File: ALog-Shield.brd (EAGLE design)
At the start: 53.3 x 78.5 mm, 25 parts, among them U1 DS3231MZ/V+T

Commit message: ALog and Made in MN back silk
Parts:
- removed U$1: ALOG_LOGO_V1_5.5MM, awickert:ALOG_LOGO_V1_SMALL
- removed U$4: NWLOGO, awickert:NWLOGO
- added LOGO1: OSHW-LOGOL, SparkFun-Aesthetics:OSHW-LOGO-L
- added U$2: MADE_IN_MN_220_SHIELD, awickert:MADE_IN_MN_SHIELD_220
- added U$3: ALOG_LOG, awickert:ALOG_LOG
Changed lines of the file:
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@@
 <text x="5.715" y="7.874" size="1.27" layer="21" rot="R90">A0</text>
 <text x="21.601" y="32.1275" size="0.6096" layer="21">TM</text>
-<text x="49.3915" y="32.146" size="0.6096" layer="21" rot="R180">TM</text>
 <text x="12.715" y="7.874" size="1.27" layer="21" rot="R90">A1</text>
 <text x="9.215" y="7.874" size="1.27" layer="21" rot="R90">3V3</text>
@@
 <element name="LED1" library="SparkFun-LED" package="LED-1206" value="" x="46.609" y="56.007"/>
 <element name="R_LED1" library="resistor" package="R0603" value="220" x="42.037" y="56.007"/>
-<element name="U$1" library="awickert" package="ALOG_LOGO_V1_SMALL" value="ALOG_LOGO_V1_5.5MM" x="20.574" y="30.48"/>
 <element name="A1" library="resistor" package="0207/10" value="" x="10.414" y="31.496"/>
-<element name="U$4" library="awickert" package="NWLOGO" value="NWLOGO" x="41.275" y="30.607"/>
 <element name="LOGO2" library="SparkFun-Aesthetics" package="OSHW-LOGO-M" value="OSHW-LOGOM" x="17.272" y="39.751"/>
 <element name="RESET" library="SparkFun-Electromechanical" package="TACTILE-PTH" value="Reset" x="49.784" y="7.62" smashed="yes" rot="R90">
@@
 <element name="C15" library="rc-master-smd" package="CECJ-CTS-031817" value="10nF" x="10.414" y="30.226" rot="R90"/>
 <element name="CLOCK_BATT" library="awickert" package="LINX_BAT-HLD-012-SMT" value="Linx BAT-HLD-012-SMT" x="6.096" y="45.72" rot="R90"/>
+<element name="U$2" library="awickert" package="MADE_IN_MN_SHIELD_220" value="MADE_IN_MN_220_SHIELD" x="42.926" y="30.226" rot="R90"/>
+<element name="U$3" library="awickert" package="ALOG_LOG" value="ALOG_LOG" x="25.146" y="35.052" rot="R90"/>
+<element name="LOGO1" library="SparkFun-Aesthetics" package="OSHW-LOGO-L" value="OSHW-LOGOL" x="-4.064" y="-45.212"/>
 </elements>
 <signals>

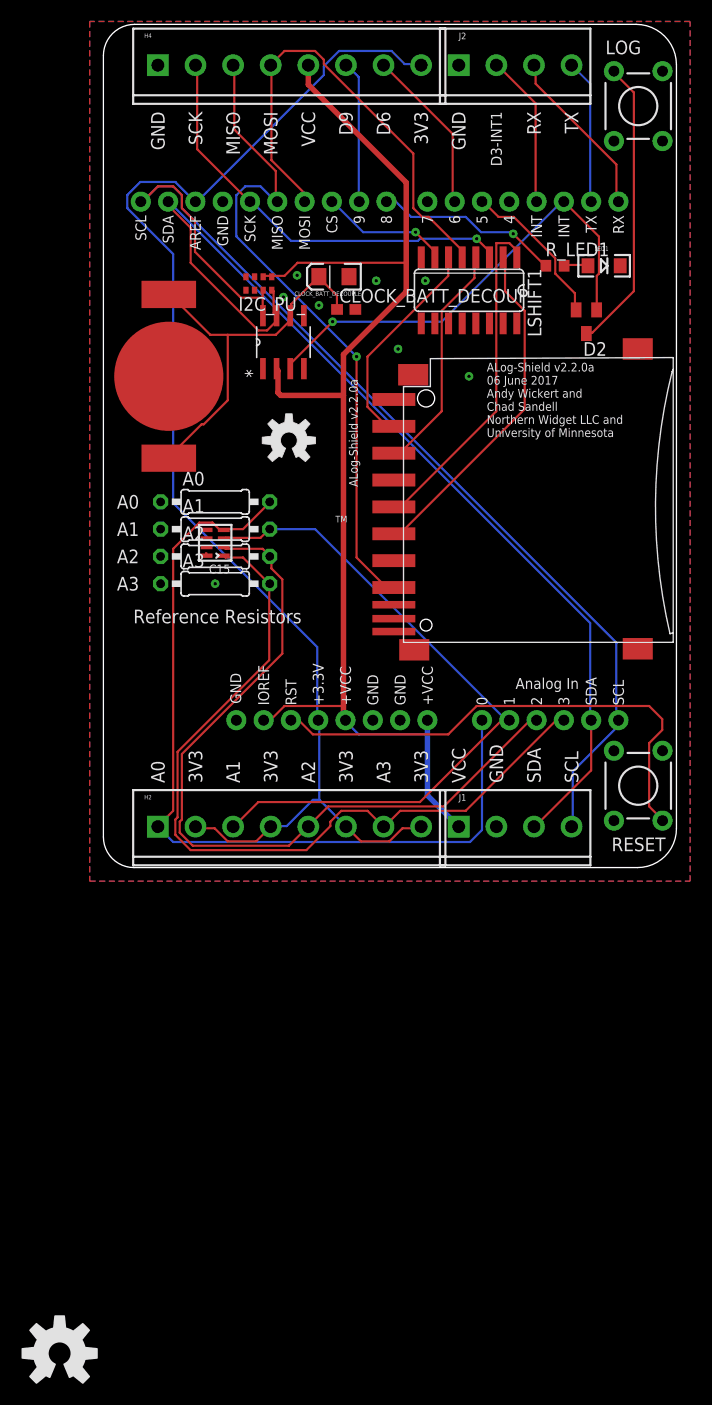
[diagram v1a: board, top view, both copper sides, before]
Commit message: Update silk and OSE logo
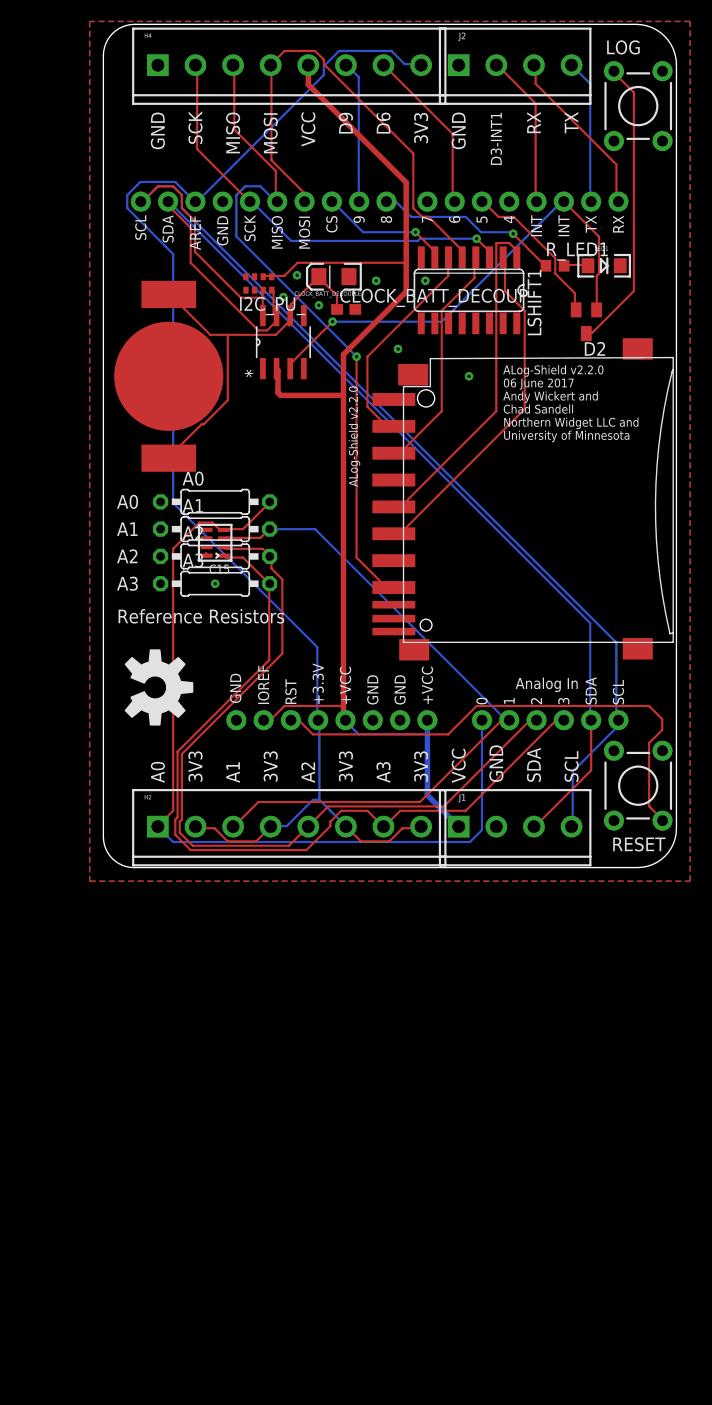
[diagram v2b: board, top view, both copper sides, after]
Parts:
- removed LOGO2: OSHW-LOGOM, SparkFun-Aesthetics:OSHW-LOGO-M
- moved LOGO1 62.6 mm to (4.83, 16.8), turned to 270 degrees
- moved U$3 5.59 mm to (19.6, 35.1)
- moved U$2 0.25 mm to (42.9, 30.5)
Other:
- board text added: "ALog-Shield v2.2.0"
- board text added: "ALog-Shield v2.2.0 06 June 2017 Andy Wickert and Chad Sandell Northern Widget LLC and University of Minnesota"
- board text removed: "ALog-Shield v2.2.0a"
- board text removed: "ALog-Shield v2.2.0a 06 June 2017 Andy Wickert and Chad Sandell Northern Widget LLC and University of Minnesota"
- board text removed: "TM"
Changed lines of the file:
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@@
 <wire x1="53.34" y1="3.62" x2="53.34" y2="74.7166" width="0" layer="20"/>
 <text x="4.445" y="70.358" size="1.27" layer="21" rot="R270">GND</text>
-<text x="35.687" y="40.0685" size="0.8128" layer="21">ALog-Shield v2.2.0a
+<text x="18.923" y="5.2705" size="0.8128" layer="22" rot="MR0">ALog-Shield v2.2.0
 06 June 2017
 Andy Wickert and
@@
 University of Minnesota</text>
 <text x="5.715" y="7.874" size="1.27" layer="21" rot="R90">A0</text>
-<text x="21.601" y="32.1275" size="0.6096" layer="21">TM</text>
 <text x="12.715" y="7.874" size="1.27" layer="21" rot="R90">A1</text>
 <text x="9.215" y="7.874" size="1.27" layer="21" rot="R90">3V3</text>
@@
 <text x="1.27" y="25.781" size="1.27" layer="21">A3</text>
 <text x="12.831" y="15.24" size="1.016" layer="21" rot="R90">GND</text>
-<text x="23.6855" y="35.433" size="0.8128" layer="21" rot="R90">ALog-Shield v2.2.0a</text>
-<text x="2.794" y="22.733" size="1.27" layer="21">Reference Resistors</text>
+<text x="23.6855" y="35.433" size="0.8128" layer="21" rot="R90">ALog-Shield v2.2.0</text>
+<text x="1.27" y="22.733" size="1.27" layer="21">Reference Resistors</text>
+<text x="37.211" y="39.8145" size="0.8128" layer="21">ALog-Shield v2.2.0
+06 June 2017
+Andy Wickert and
+Chad Sandell
+Northern Widget LLC and
+University of Minnesota</text>
 </plain>
 <attributes>
@@
 <element name="R_LED1" library="resistor" package="R0603" value="220" x="42.037" y="56.007"/>
 <element name="A1" library="resistor" package="0207/10" value="" x="10.414" y="31.496"/>
-<element name="LOGO2" library="SparkFun-Aesthetics" package="OSHW-LOGO-M" value="OSHW-LOGOM" x="17.272" y="39.751"/>
 <element name="RESET" library="SparkFun-Electromechanical" package="TACTILE-PTH" value="Reset" x="49.784" y="7.62" smashed="yes" rot="R90">
 <attribute name="PROD_ID" value=" SWCH-08441" x="218.694" y="-81.28" size="1.778" layer="27" rot="R90" display="off"/>
@@
 <element name="C15" library="rc-master-smd" package="CECJ-CTS-031817" value="10nF" x="10.414" y="30.226" rot="R90"/>
 <element name="CLOCK_BATT" library="awickert" package="LINX_BAT-HLD-012-SMT" value="Linx BAT-HLD-012-SMT" x="6.096" y="45.72" rot="R90"/>
-<element name="U$2" library="awickert" package="MADE_IN_MN_SHIELD_220" value="MADE_IN_MN_220_SHIELD" x="42.926" y="30.226" rot="R90"/>
-<element name="U$3" library="awickert" package="ALOG_LOG" value="ALOG_LOG" x="25.146" y="35.052" rot="R90"/>
-<element name="LOGO1" library="SparkFun-Aesthetics" package="OSHW-LOGO-L" value="OSHW-LOGOL" x="-4.064" y="-45.212"/>
+<element name="U$2" library="awickert" package="MADE_IN_MN_SHIELD_220" value="MADE_IN_MN_220_SHIELD" x="42.926" y="30.48" rot="R90"/>
+<element name="U$3" library="awickert" package="ALOG_LOG" value="ALOG_LOG" x="19.558" y="35.052" rot="R90"/>
+<element name="LOGO1" library="SparkFun-Aesthetics" package="OSHW-LOGO-L" value="OSHW-LOGOL" x="4.826" y="16.764" rot="R270"/>
 </elements>
 <signals>

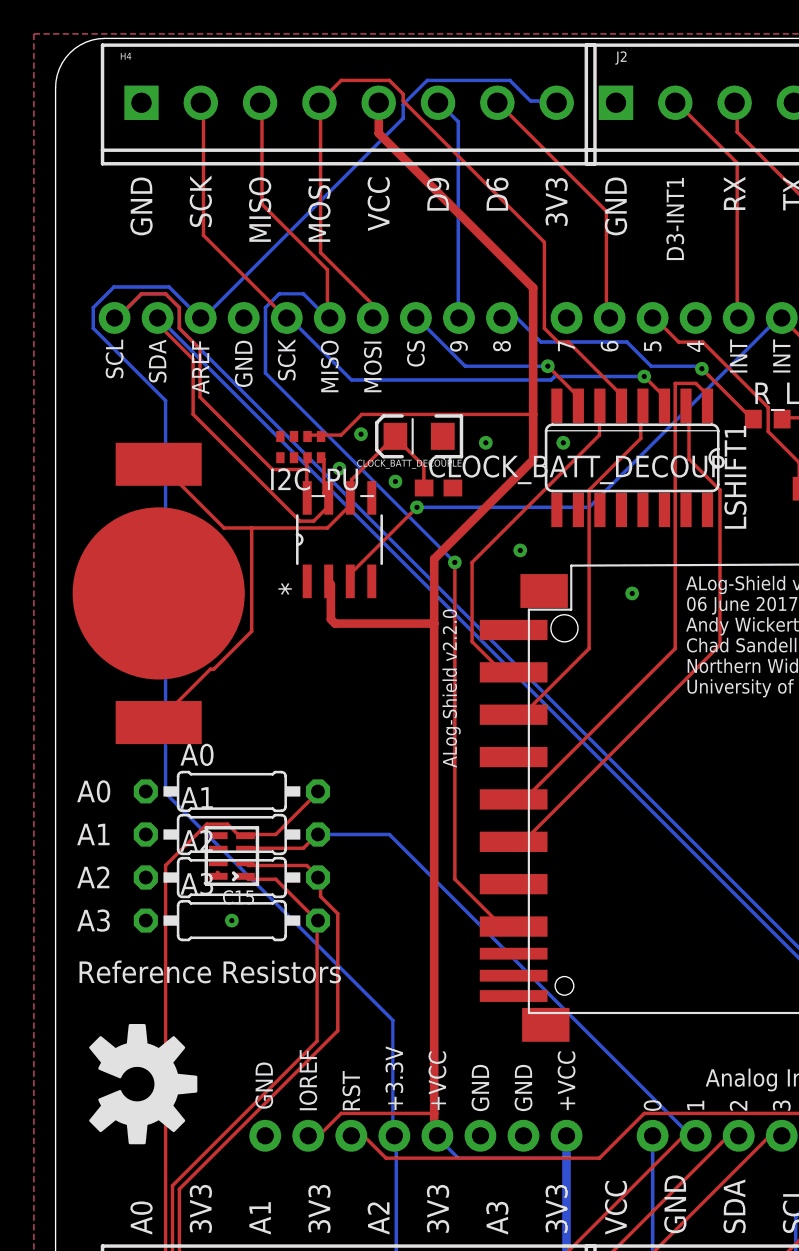
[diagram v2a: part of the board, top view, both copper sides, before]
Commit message: Added D4 and D7 out put points, will not populate with screw terminals
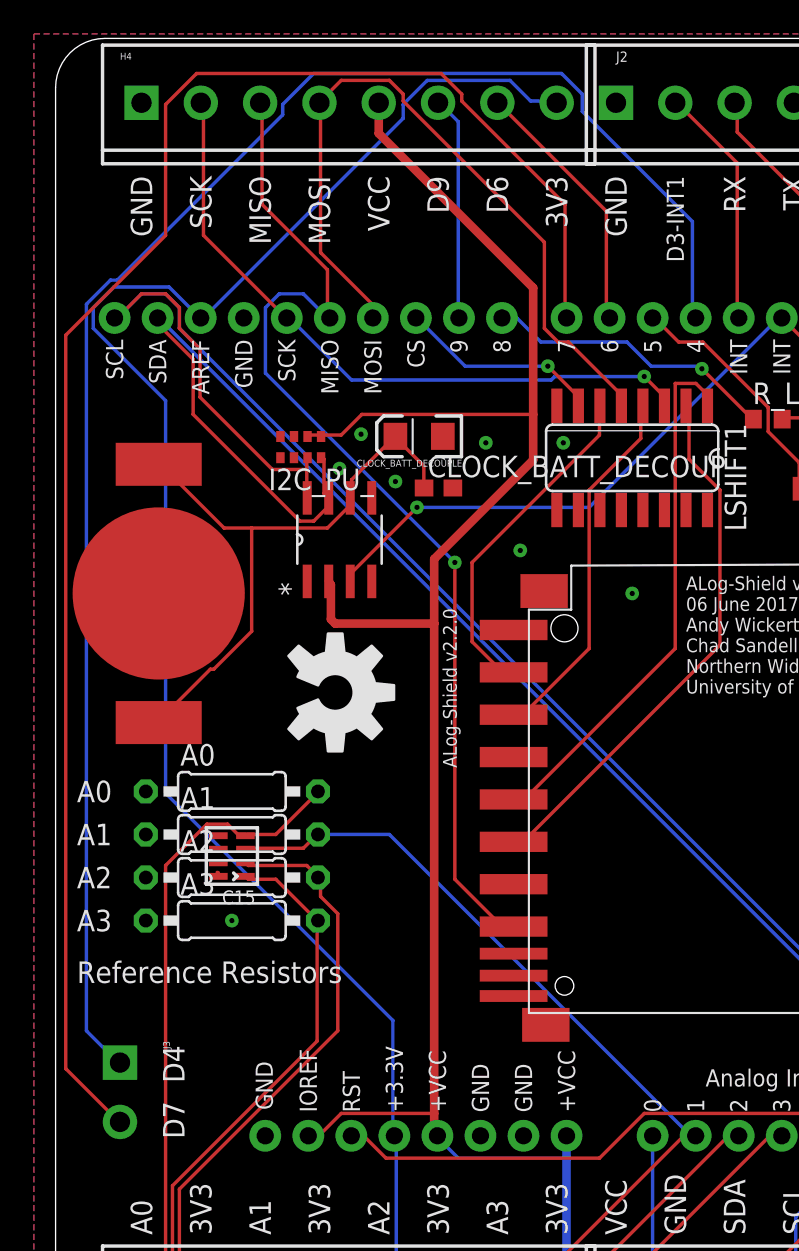
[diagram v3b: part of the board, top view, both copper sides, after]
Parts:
- added J3: (no value), SparkFun-Connectors:SCREWTERMINAL-3.5MM-2-NS
- moved LOGO1 25.9 mm to (16.5, 39.9)
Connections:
- removed net D4-SENSE_LDO_SWITCH: U$9.D4
- removed net D7-CLOCK_SD_SWITCH: U$9.D7
- new net D4: J3.1, U$9.D4
- new net D7: J3.2, U$9.D7
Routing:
- net D7: track 0.00 -> 98.4 mm
- net D4: track 0.00 -> 97.5 mm
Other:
- board text added: "D4"
- board text added: "D7"
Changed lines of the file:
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@@
 <layer number="49" name="Reference" color="7" fill="1" visible="yes" active="yes"/>
 <layer number="50" name="dxf" color="7" fill="1" visible="yes" active="yes"/>
-<layer number="51" name="tDocu" color="7" fill="1" visible="yes" active="yes"/>
+<layer number="51" name="tDocu" color="7" fill="1" visible="no" active="yes"/>
 <layer number="52" name="bDocu" color="7" fill="1" visible="yes" active="yes"/>
 <layer number="53" name="tGND_GNDA" color="7" fill="9" visible="no" active="no"/>
@@
 Northern Widget LLC and
 University of Minnesota</text>
+<text x="6.35" y="19.05" size="1.27" layer="21" rot="R270">D4</text>
+<text x="6.35" y="15.748" size="1.27" layer="21" rot="R270">D7</text>
 </plain>
 <attributes>
@@
 <element name="U$2" library="awickert" package="MADE_IN_MN_SHIELD_220" value="MADE_IN_MN_220_SHIELD" x="42.926" y="30.48" rot="R90"/>
 <element name="U$3" library="awickert" package="ALOG_LOG" value="ALOG_LOG" x="19.558" y="35.052" rot="R90"/>
-<element name="LOGO1" library="SparkFun-Aesthetics" package="OSHW-LOGO-L" value="OSHW-LOGOL" x="4.826" y="16.764" rot="R270"/>
+<element name="LOGO1" library="SparkFun-Aesthetics" package="OSHW-LOGO-L" value="OSHW-LOGOL" x="16.51" y="39.878" rot="R270"/>
+<element name="J3" library="SparkFun-Connectors" package="SCREWTERMINAL-3.5MM-2-NS" value="" x="3.81" y="18.034" rot="R270">
+<attribute name="PROD_ID" value="CONN-08399" x="3.81" y="18.034" size="1.778" layer="27" rot="R270" display="off"/>
+</element>
 </elements>
 <signals>
@@
 <wire x1="47.5488" y1="73.9648" x2="47.5234" y2="74.1172" width="0.2032" layer="1"/>
 </signal>
-<signal name="D4-SENSE_LDO_SWITCH">
+<signal name="D4">
 <contactref element="U$9" pad="D4"/>
+<contactref element="J3" pad="1"/>
+<wire x1="37.592" y1="67.6656" x2="37.592" y2="61.976" width="0.2032" layer="16"/>
+<wire x1="31.0896" y1="74.168" x2="37.592" y2="67.6656" width="0.2032" layer="16"/>
+<wire x1="31.0896" y1="75.184" x2="31.0896" y2="74.168" width="0.2032" layer="16"/>
+<wire x1="29.8704" y1="76.4032" x2="31.0896" y2="75.184" width="0.2032" layer="16"/>
+<wire x1="15.24" y1="76.4032" x2="29.8704" y2="76.4032" width="0.2032" layer="16"/>
+<wire x1="13.4112" y1="74.5744" x2="15.24" y2="76.4032" width="0.2032" layer="16"/>
+<wire x1="13.4112" y1="73.9648" x2="13.4112" y2="74.5744" width="0.2032" layer="16"/>
+<wire x1="3.6576" y1="64.2112" x2="13.4112" y2="73.9648" width="0.2032" layer="16"/>
+<wire x1="3.2512" y1="64.2112" x2="3.6576" y2="64.2112" width="0.2032" layer="16"/>
+<wire x1="1.8288" y1="62.7888" x2="3.2512" y2="64.2112" width="0.2032" layer="16"/>
+<wire x1="1.8288" y1="19.9136" x2="1.8288" y2="62.7888" width="0.2032" layer="16"/>
+<wire x1="3.6576" y1="18.0848" x2="1.8288" y2="19.9136" width="0.2032" layer="16"/>
+<wire x1="37.592" y1="61.976" x2="37.7825" y2="61.976" width="0.2032" layer="16"/>
+<wire x1="3.6576" y1="18.0848" x2="3.81" y2="18.034" width="0.2032" layer="16"/>
 </signal>
 <signal name="D6-EXT">
@@
 <wire x1="22.7584" y1="74.5744" x2="22.58" y2="74.676" width="0.2032" layer="16"/>
 </signal>
-<signal name="D7-CLOCK_SD_SWITCH">
+<signal name="D7">
 <contactref element="U$9" pad="D7"/>
+<contactref element="J3" pad="2"/>
+<wire x1="30.0736" y1="68.6816" x2="30.0736" y2="61.976" width="0.2032" layer="1"/>
+<wire x1="23.9776" y1="74.7776" x2="30.0736" y2="68.6816" width="0.2032" layer="1"/>
+<wire x1="23.9776" y1="75.184" x2="23.9776" y2="74.7776" width="0.2032" layer="1"/>
+<wire x1="22.7584" y1="76.4032" x2="23.9776" y2="75.184" width="0.2032" layer="1"/>
+<wire x1="8.3312" y1="76.4032" x2="22.7584" y2="76.4032" width="0.2032" layer="1"/>
+<wire x1="6.5024" y1="74.5744" x2="8.3312" y2="76.4032" width="0.2032" layer="1"/>
+<wire x1="6.5024" y1="66.8528" x2="6.5024" y2="74.5744" width="0.2032" layer="1"/>
+<wire x1="0.6096" y1="60.96" x2="6.5024" y2="66.8528" width="0.2032" layer="1"/>
+<wire x1="0.6096" y1="17.6784" x2="0.6096" y2="60.96" width="0.2032" layer="1"/>
+<wire x1="3.6576" y1="14.6304" x2="0.6096" y2="17.6784" width="0.2032" layer="1"/>
+<wire x1="30.0736" y1="61.976" x2="30.1625" y2="61.976" width="0.2032" layer="1"/>
+<wire x1="3.6576" y1="14.6304" x2="3.81" y2="14.534" width="0.2032" layer="1"/>
 </signal>
 </signals>

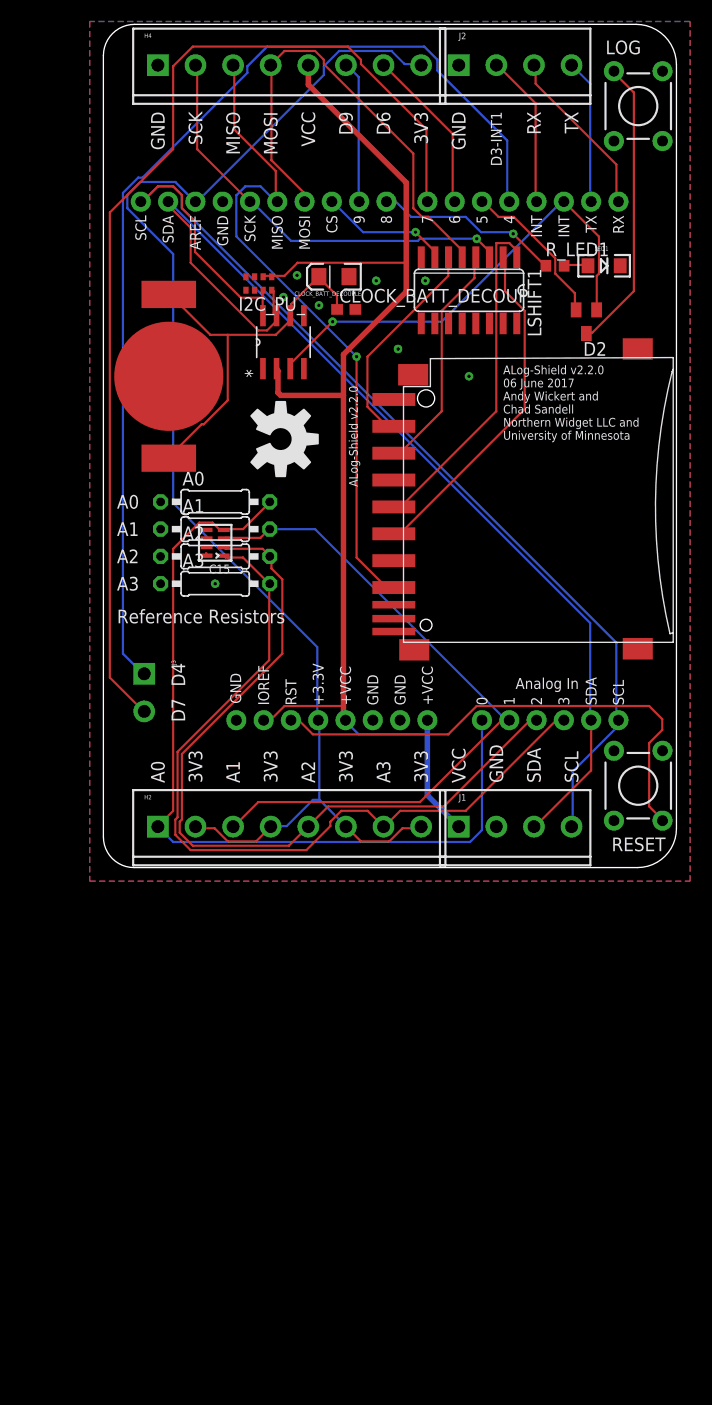
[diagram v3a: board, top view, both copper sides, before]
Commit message: changes made to allow OSH Park board run
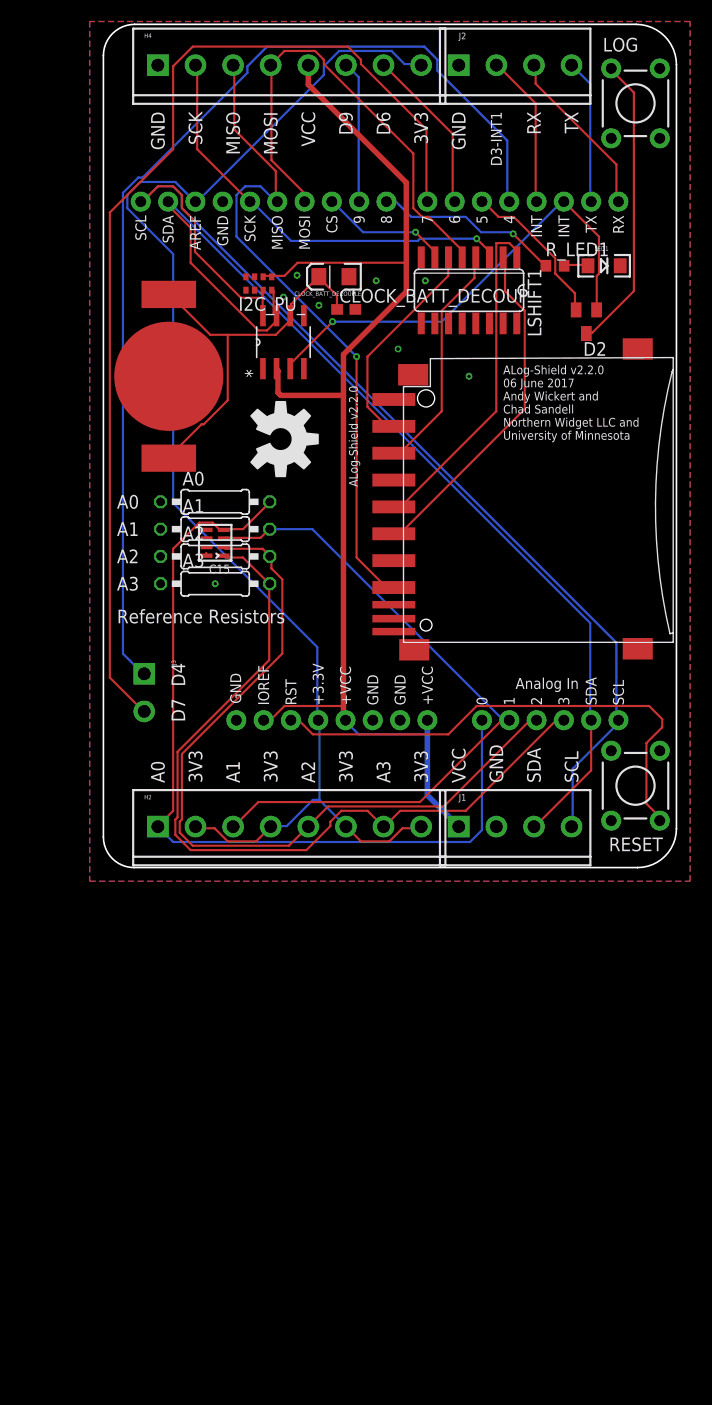
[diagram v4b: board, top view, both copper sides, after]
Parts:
- moved LOG 0.36 mm to (49.5, 71.1)
- moved RESET 0.25 mm to (49.5, 7.62)
